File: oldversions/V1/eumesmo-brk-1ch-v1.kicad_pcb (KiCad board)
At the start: 2 copper layers, 22 x 28 mm, 2 parts, among them J1 RJ45, J2 1x4P 5,08 SCREW

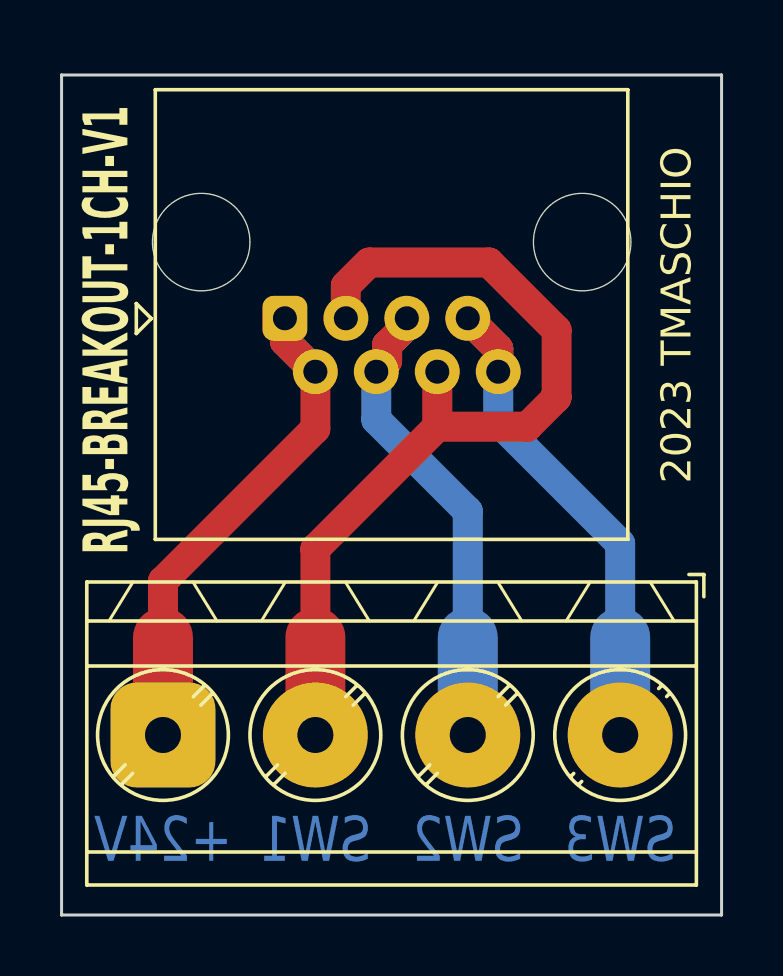
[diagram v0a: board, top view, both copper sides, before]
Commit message: Moved old versions to the oldversions folder.
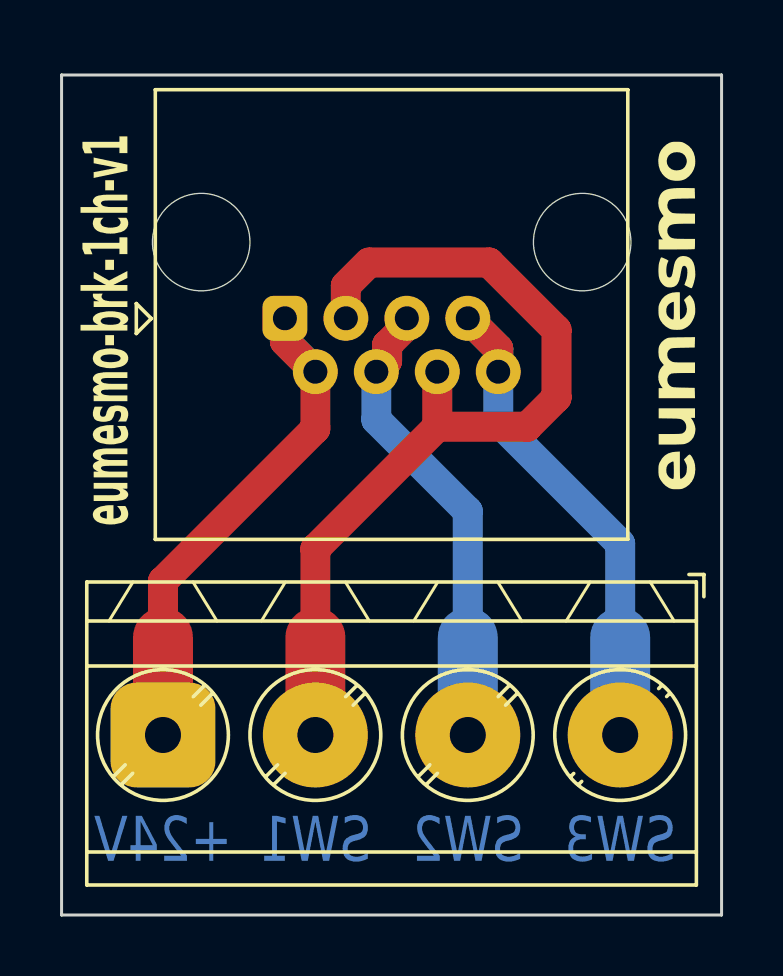
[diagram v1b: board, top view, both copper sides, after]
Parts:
- added G***: LOGO, Tales:Eumesmo_small_silk, F.Cu at (148.5, 100.0)
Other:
- board text added: "eumesmo-brk-1ch-v1"
- board text removed: "2023 TMASCHIO"
- board text removed: "RJ45-BREAKOUT-1CH-V1"
